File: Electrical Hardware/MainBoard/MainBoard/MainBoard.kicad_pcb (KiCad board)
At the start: 2 copper layers, 51.2 x 51.7 mm, 78 parts, among them J1 SM02B-SRSS-TB_LFSN_, J11 USB4500-03-0-A_REVA1, J2 Conn_01x04_Socket, J3 Conn_01x04_Socket, J4 Conn_01x04_Socket, J6 Thermistor, J7 62684-401100ALF, J8 Conn_01x02_Socket, SW1 SW_Push, SW2 SW_Push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

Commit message: Make layout edits
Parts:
- moved JP6 2.65 mm to (73.5, 59.2), turned to 30 degrees
- moved JP8 2.51 mm to (74.8, 61.3), turned to 30 degrees
- moved JP7 2.29 mm to (76.1, 63.5), turned to 30 degrees
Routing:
- net Net-(J11-VBUS_A): track 12.5 -> 2.94 mm
- net GND: track 135.2 -> 129.4 mm
- net Net-(JP6-C): track 12.6 -> 15.8 mm
- net Net-(JP8-C): track 15.6 -> 17.5 mm
- net Net-(JP7-C): track 20.7 -> 22.5 mm
- net Net-(J11-CC1): track 0.00 -> 1.54 mm

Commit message: Mess around with layout
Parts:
- moved R21 2.16 mm to (78.5, 51.2)
- moved R20 1.27 mm to (78.5, 49.7)
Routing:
- net D+: track 14.8 -> 19.5 mm
- net Net-(J11-CC2): track 0.00 -> 3.42 mm
- net Net-(J11-CC1): track 1.54 -> 3.34 mm
- net D-: track 18.6 -> 20.0 mm
- net Net-(D2-K): track 10.3 -> 9.53 mm

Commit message: IM ABOUT TO YEET DIS BITCH
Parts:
- moved CR1 5.62 mm to (82.8, 49.8), turned to 180 degrees
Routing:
- net Net-(U4-ISET): track 6.04 -> 0.00 mm
- net Net-(U4-ITERM): track 5.79 -> 0.00 mm
- net Net-(U4-TMR): track 5.56 -> 0.00 mm
- net D+: track 19.5 -> 15.9 mm
- net D-: track 20.0 -> 16.8 mm
- net Net-(J11-VBUS_A): track 2.94 -> 0.00 mm
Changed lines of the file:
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@@
   )
   (footprint "MBRA140TRPBF:DIODE_SMA_VIS-L" (layer "F.Cu")
-    (at 85.972407 45.137508 -90)
+    (at 82.804 49.784 180)
     (tags "VS-MBRA140TRPBF ")
     (property "Sheetfile" "MainBoard.kicad_sch")
@@
     (property "ki_keywords" "VS-MBRA140TRPBF")
     (attr smd)
-    (fp_text reference "CR1" (at 0.074492 -2.419593 90 unlocked) (layer "F.SilkS")
+    (fp_text reference "CR1" (at 0.074492 -2.419593 unlocked) (layer "F.SilkS")
         (effects (font (size 0.75 0.75) (thickness 0.15)))
     )
-    (fp_text value "VS-MBRA140TRPBF" (at 0 0 -90 unlocked) (layer "F.Fab")
+    (fp_text value "VS-MBRA140TRPBF" (at 0 0 180 unlocked) (layer "F.Fab")
         (effects (font (size 1 1) (thickness 0.15)))
     )
-    (fp_text user "${REFERENCE}" (at 0 0 -90 unlocked) (layer "F.Fab")
+    (fp_text user "${REFERENCE}" (at 0 0 180 unlocked) (layer "F.Fab")
         (effects (font (size 1 1) (thickness 0.15)))
     )
@@
     (fp_line (start 2.6416 1.4478) (end 2.6416 -1.4478)
       (stroke (width 0.0254) (type solid)) (layer "F.Fab"))
-    (pad "1" smd rect (at -1.8161 0) (size 1.524 1.8034) (layers "F.Cu" "F.Paste" "F.Mask")
+    (pad "1" smd rect (at -1.8161 0 270) (size 1.524 1.8034) (layers "F.Cu" "F.Paste" "F.Mask")
       (net 6 "+5V_IN") (pintype "unspecified"))
-    (pad "2" smd rect (at 1.8161 0) (size 1.524 1.8034) (layers "F.Cu" "F.Paste" "F.Mask")
+    (pad "2" smd rect (at 1.8161 0 270) (size 1.524 1.8034) (layers "F.Cu" "F.Paste" "F.Mask")
       (net 83 "Net-(J11-VBUS_A)") (pintype "unspecified"))
     (zone (net 0) (net_name "") (layer "F.Cu") (hatch full 0.508)
@@
       (polygon
         (pts
-          (xy 85.134207 42.546708)
-          (xy 85.134207 47.728308)
-          (xy 84.575407 47.728308)
-          (xy 84.575407 42.546708)
+          (xy 83.6676 50.622199)
+          (xy 81.9404 50.622199)
+          (xy 81.9404 48.945801)
+          (xy 83.6676 48.945801)
         )
       )
@@
       (polygon
         (pts
-          (xy 86.810606 44.273908)
-          (xy 86.810606 46.001108)
-          (xy 85.134208 46.001108)
-          (xy 85.134208 44.273908)
+          (xy 85.3948 48.9458)
+          (xy 80.2132 48.9458)
+          (xy 80.2132 48.387)
+          (xy 85.3948 48.387)
         )
       )
@@
       (polygon
         (pts
-          (xy 87.369407 42.546708)
-          (xy 87.369407 47.728308)
-          (xy 86.810607 47.728308)
-          (xy 86.810607 42.546708)
+          (xy 85.3948 51.181)
+          (xy 80.2132 51.181)
+          (xy 80.2132 50.6222)
+          (xy 85.3948 50.6222)
         )
       )
@@
   (segment (start 87.521807 42.841015) (end 87.521807 48.004013) (width 0.3048) (layer "F.Cu") (net 26))
   (segment (start 94.7354 42.3308) (end 94.7354 41.5754) (width 0.4064) (layer "F.Cu") (net 26))
-  (segment (start 87.521807 48.004013) (end 85.26412 50.2617) (width 0.3048) (layer "F.Cu") (net 26))
   (segment (start 92.6116 40.3574) (end 91.5291 41.4399) (width 0.3048) (layer "F.Cu") (net 26))
   (segment (start 88.922922 41.4399) (end 87.521807 42.841015) (width 0.3048) (layer "F.Cu") (net 26))
@@
   (segment (start 88.026607 43.193794) (end 89.275701 41.9447) (width 0.3048) (layer "F.Cu") (net 27))
   (segment (start 75.819 51.943) (end 76.29796 51.943) (width 0.2) (layer "F.Cu") (net 27))
-  (segment (start 85.4717 50.9117) (end 88.026607 48.356793) (width 0.3048) (layer "F.Cu") (net 27))
   (segment (start 76.708 50.927) (end 76.4417 50.6607) (width 0.2) (layer "F.Cu") (net 27))
   (segment (start 76.4417 50.6607) (end 74.85 50.6607) (width 0.2) (layer "F.Cu") (net 27))
@@
   (segment (start 102.224543 61.3867) (end 103.0717 61.3867) (width 0.2032) (layer "B.Cu") (net 36))
   (segment (start 100.220818 63.390425) (end 102.224543 61.3867) (width 0.2032) (layer "B.Cu") (net 36))
-  (segment (start 79.2717 43.2617) (end 79.2717 43.8992) (width 0.254) (layer "F.Cu") (net 37))
-  (segment (start 77.7547 42.3947) (end 77.9717 42.6117) (width 0.254) (layer "F.Cu") (net 37))
-  (segment (start 78.0967 40.2367) (end 77.7547 40.5787) (width 0.254) (layer "F.Cu") (net 37))
-  (segment (start 77.9717 42.6117) (end 78.6217 42.6117) (width 0.254) (layer "F.Cu") (net 37))
-  (segment (start 78.0967 39.4867) (end 78.0967 40.2367) (width 0.254) (layer "F.Cu") (net 37))
-  (segment (start 77.7547 40.5787) (end 77.7547 42.3947) (width 0.254) (layer "F.Cu") (net 37))
-  (segment (start 78.6217 42.6117) (end 79.2717 43.2617) (width 0.254) (layer "F.Cu") (net 37))
-  (segment (start 74.9217 40.216409) (end 76.8467 42.141409) (width 0.254) (layer "F.Cu") (net 38))
-  (segment (start 77.8592 43.8992) (end 78.2717 43.8992) (width 0.254) (layer "F.Cu") (net 38))
-  (segment (start 76.8467 42.8867) (end 77.8592 43.8992) (width 0.254) (layer "F.Cu") (net 38))
-  (segment (start 74.9217 39.4867) (end 74.9217 40.216409) (width 0.254) (layer "F.Cu") (net 38))
-  (segment (start 76.8467 42.141409) (end 76.8467 42.8867) (width 0.254) (layer "F.Cu") (net 38))
   (segment (start 81.5467 43.8617) (end 82.1717 43.8617) (width 0.25) (layer "F.Cu") (net 39))
   (segment (start 80.4592 44.5867) (end 80.8217 44.5867) (width 0.25) (layer "F.Cu") (net 39))
   (segment (start 80.8217 44.5867) (end 81.5467 43.8617) (width 0.25) (layer "F.Cu") (net 39))
-  (segment (start 78.7717 43.410864) (end 78.7717 43.8992) (width 0.254) (layer "F.Cu") (net 40))
-  (segment (start 76.5217 39.4867) (end 76.5217 41.174357) (width 0.254) (layer "F.Cu") (net 40))
-  (segment (start 76.5217 41.174357) (end 77.3007 41.953357) (width 0.254) (layer "F.Cu") (net 40))
-  (segment (start 78.472536 43.1117) (end 78.7717 43.410864) (width 0.254) (layer "F.Cu") (net 40))
-  (segment (start 77.713752 43.1117) (end 78.472536 43.1117) (width 0.254) (layer "F.Cu") (net 40))
-  (segment (start 77.3007 42.698648) (end 77.713752 43.1117) (width 0.254) (layer "F.Cu") (net 40))
-  (segment (start 77.3007 41.953357) (end 77.3007 42.698648) (width 0.254) (layer "F.Cu") (net 40))
   (segment (start 98.1967 28.0117) (end 96.3467 28.0117) (width 0.254) (layer "F.Cu") (net 41))
   (segment (start 98.8967 28.7117) (end 98.1967 28.0117) (width 0.254) (layer "F.Cu") (net 41))
@@
   (segment (start 110.146698 66.736702) (end 110.146698 61.8617) (width 0.2032) (layer "B.Cu") (net 78))
   (segment (start 86.717416 65.9117) (end 86.717416 67.127626) (width 0.2032) (layer "B.Cu") (net 78))
-  (segment (start 84.805277 49.4117) (end 85.9717 48.245277) (width 0.8128) (layer "F.Cu") (net 83))
-  (segment (start 85.9717 48.245277) (end 85.9717 46.9529) (width 0.8128) (layer "F.Cu") (net 83))
   (segment (start 75.5613 49.6607) (end 74.85 49.6607) (width 0.25) (layer "F.Cu") (net 84))
   (segment (start 77.026 49.022) (end 76.2 49.022) (width 0.25) (layer "F.Cu") (net 84))

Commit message: YEETED THA BITCH
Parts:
- moved D3 58.8 mm to (32.4, 95.8)
- moved U7 58.8 mm to (35.2, 91.6)
- moved C12 58.8 mm to (35.6, 88.7)
- moved C17 58.8 mm to (37.4, 93.4)
- moved R17 58.8 mm to (38.9, 93.4)
- moved C16 58.8 mm to (35.5, 94.9)
- moved L2 58.8 mm to (31.0, 91.4)
- moved R15 58.8 mm to (38.1, 90.8)
- moved R16 58.8 mm to (38.8, 89.3)
- moved D2 58.3 mm to (22.3, 47.0)
- moved D1 58.3 mm to (22.3, 48.6)
- moved R10 58.2 mm to (25.3, 48.6)
- moved R11 58.2 mm to (25.3, 47.0)
- moved C2 54.7 mm to (20.8, 41.4)
- moved R1 54.7 mm to (21.1, 39.0)
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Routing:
- net +3.3V: track 144.9 -> 6.62 mm, vias 6 -> 1
- net GND: track 129.4 -> 25.1 mm, vias 64 -> 29
- net /SDA: track 69.5 -> 0.00 mm, vias 4 -> 0
- net /SCL: track 66.2 -> 0.00 mm, vias 3 -> 0
- net /TFT_RESET: track 56.5 -> 0.00 mm, vias 3 -> 0
- net /TP_IRQ: track 54.6 -> 0.00 mm, vias 2 -> 0
- net +4V4: track 50.3 -> 3.79 mm, vias 6 -> 2
- net /BOOT0_B4: track 38.9 -> 0.00 mm, vias 2 -> 0
- net +24V: track 32.9 -> 1.27 mm, vias 1 -> 0
- net /LEDK: track 30.4 -> 0.00 mm, vias 1 -> 0
- net /BTN_1: track 28.4 -> 0.00 mm, vias 1 -> 0
- net A1: track 28.2 -> 0.00 mm
- net /R5: track 25.4 -> 0.00 mm, vias 1 -> 0
- net /R4: track 24.1 -> 0.00 mm, vias 1 -> 0
- net /ADDR2: track 23.9 -> 0.00 mm
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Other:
- outline, holes or cut-outs redrawn

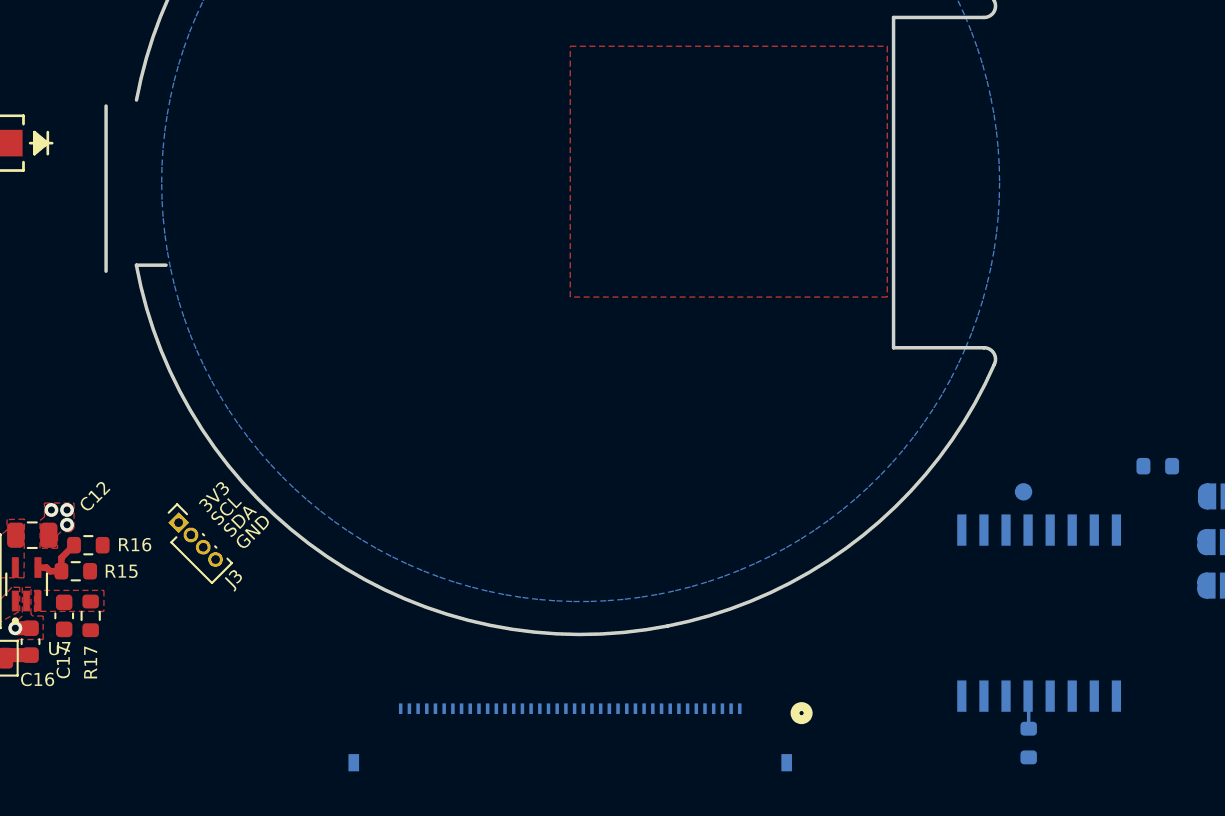
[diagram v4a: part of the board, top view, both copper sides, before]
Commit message: Add smaller gpio expander footprint
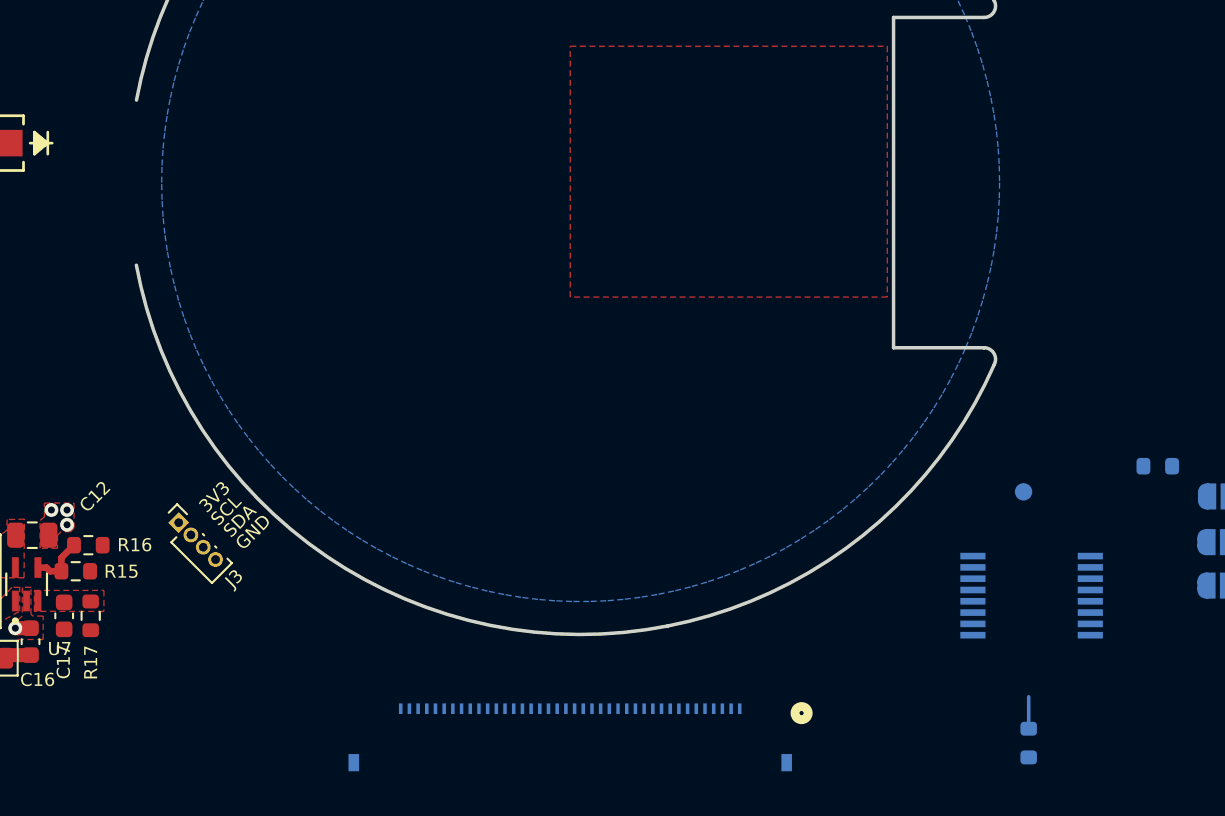
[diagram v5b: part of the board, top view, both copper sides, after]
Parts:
- U3: footprint PCA9554AD:SOT162-1_NXP -> PCA9554AD:SOT338-1_NXP-L
- moved U3 1.09 mm to (93.0, 92.2), turned to 180 degrees
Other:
- board size 51.2 x 51.7 mm -> 49.4 x 51.7 mm

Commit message: Make slow moves to un-yeet
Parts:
- moved R14 32.7 mm to (155.4, 86.8)
- moved TP1 32.7 mm to (143.0, 88.5)
- moved TP3 32.7 mm to (140.5, 88.5)
- moved TP2 32.7 mm to (141.7, 90.1)
- moved R9 30.6 mm to (137.9, 48.9)
- moved U2 30.6 mm to (142.2, 43.9)
- moved C4 30.6 mm to (144.5, 43.4)
- moved C6 30.6 mm to (142.7, 43.4)
- moved C8 30.6 mm to (144.4, 43.5)
- moved J4 30.6 mm to (148.9, 49.0)
- moved R4 30.6 mm to (140.4, 48.1)
- moved J2 30.6 mm to (130.4, 49.1)
- moved U1 28.8 mm to (90.0, 65.0)
- moved J7 26.7 mm to (64.7, 74.6), turned to 90 degrees
- moved JP2 23.8 mm to (128.1, 92.0)
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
